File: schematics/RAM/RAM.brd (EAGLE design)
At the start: 134.9 x 102.5 mm, 31 parts

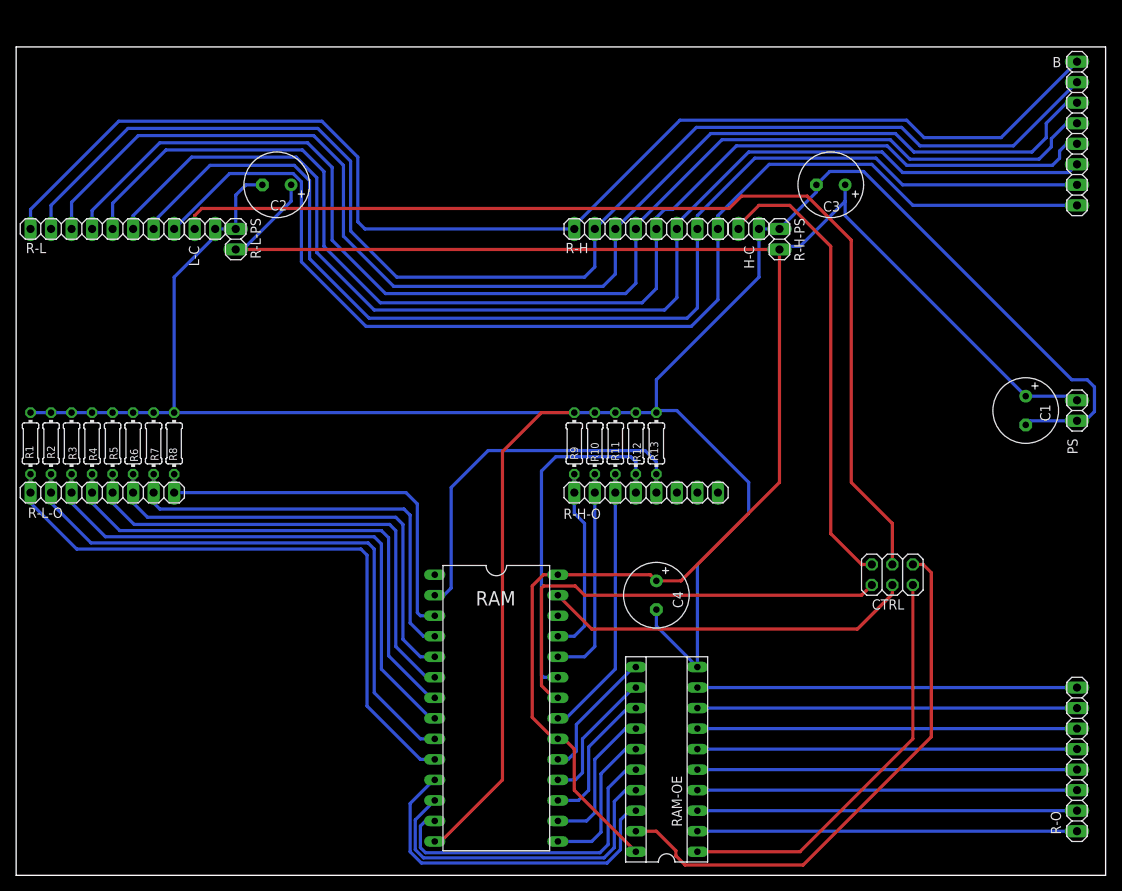
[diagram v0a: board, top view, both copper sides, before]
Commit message: RAM merged with register.
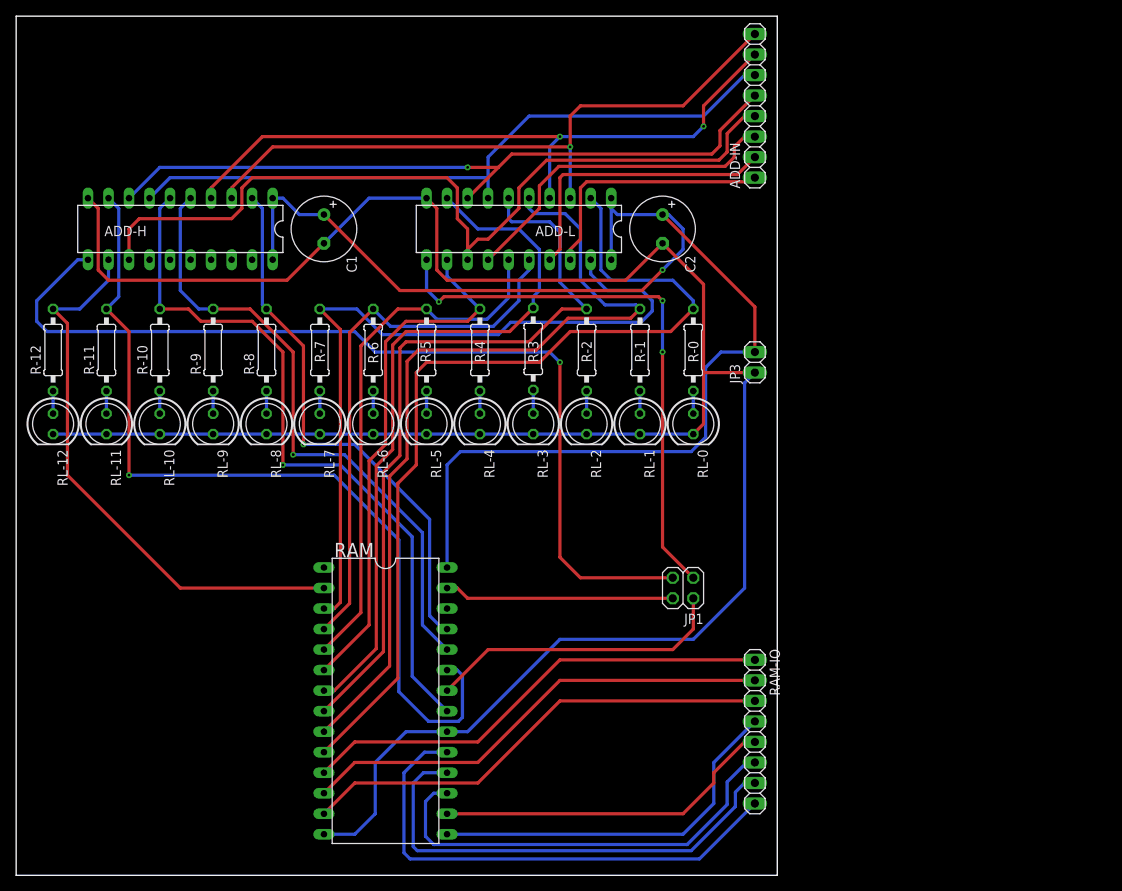
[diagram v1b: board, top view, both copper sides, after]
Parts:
- removed B, R-H, R-H-O, R-L, R-L-O, R-O: (no value), pinhead:1X08
- removed C3, C4: (no value), rcl:E3,5-8
- removed CTRL: (no value), pinhead:2X03
- removed H-C, L-C, PS, R-H-PS, R-L-PS: (no value), pinhead:1X02
- removed R1, R10, R11, R12, R13, R2, R3, R4, R5, R6, R7, R8, R9: (no value), rcl:0204/7
- removed RAM-OE: (no value), ic-package:SOCKET-20
- added ADD-H, ADD-L: 74273N, 74ttl-din:DIL20
- added ADD-IN, RAM-IO: (no value), pinhead:1X08
- added JP1: (no value), pinhead:2X02
- added JP3: (no value), pinhead:1X02
- added R-0, R-1, R-10, R-11, R-12, R-2, R-3, R-4, R-5, R-6, R-7, R-8, R-9: (no value), rcl:0207/10
- added RL-0, RL-1, RL-10, RL-11, RL-12, RL-2, RL-3, RL-4, RL-5, RL-6, RL-7, RL-8, RL-9: (no value), led:LED5MM
- RAM: device ic-package:DIL28-6 -> memory-nec:DIL28-6
- moved C1 89.7 mm to (38.1, 80.0)
- moved C2 48.1 mm to (80.0, 80.0), turned to 270 degrees
- moved RAM 13.7 mm to (45.7, 21.6)
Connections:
- removed net B0: B.8, R-H.1, R-L.1
- removed net B1: B.7, R-H.2, R-L.2
- removed net B2: B.6, R-H.3, R-L.3
- removed net B3: B.5, R-H.4, R-L.4
- removed net B4: B.4, R-H.5, R-L.5
- removed net B5: B.3, R-H.6, R-L.6
- removed net B6: B.2, R-H.7, R-L.7
- removed net B7: B.1, R-H.8, R-L.8
- removed net OE-DIR: CTRL.5, RAM-OE.1
- removed net R-H-CP: CTRL.2, H-C.2
- removed net R-L-CP: CTRL.4, L-C.2
- removed net R0: R-O.8, RAM-OE.2
- removed net R1: R-O.7, RAM-OE.3
- removed net R2: R-O.6, RAM-OE.4
- removed net R3: R-O.5, RAM-OE.5
- removed net R4: R-O.4, RAM-OE.6
- removed net R5: R-O.3, RAM-OE.7
- removed net R6: R-O.2, RAM-OE.8
- removed net R7: R-O.1, RAM-OE.9
- removed net RA0: R-L-O.1, R1.1, RAM.10
- removed net RA1: R-L-O.2, R2.1, RAM.9
- removed net RA10: R-H-O.3, R11.1, RAM.21
- removed net RA11: R-H-O.4, R12.1, RAM.23
- removed net RA12: R-H-O.5, R13.1, RAM.2
- removed net RA2: R-L-O.3, R3.1, RAM.8
- removed net RA3: R-L-O.4, R4.1, RAM.7
- removed net RA4: R-L-O.5, R5.1, RAM.6
- removed net RA5: R-L-O.6, R6.1, RAM.5
- removed net RA6: R-L-O.7, R7.1, RAM.4
- removed net RA7: R-L-O.8, R8.1, RAM.3
- removed net RA8: R-H-O.1, R9.1, RAM.25
- removed net RA9: R-H-O.2, R10.1, RAM.24
- removed net RAM-OE: CTRL.1, RAM.22
- removed net RAM0: RAM-OE.18, RAM.11
- removed net RAM1: RAM-OE.17, RAM.12
- removed net RAM2: RAM-OE.16, RAM.13
- removed net RAM3: RAM-OE.15, RAM.15
- removed net RAM4: RAM-OE.14, RAM.16
- removed net RAM5: RAM-OE.13, RAM.17
- removed net RAM6: RAM-OE.12, RAM.18
- removed net RAM7: RAM-OE.11, RAM.19
- new net ADD-H-CP: ADD-H.11, JP1.3
- new net ADD-L-CP: ADD-L.11, JP1.1
- new net BI-0: ADD-H.3, ADD-IN.8, ADD-L.3
- new net BI-1: ADD-H.4, ADD-IN.7, ADD-L.4
- new net BI-2: ADD-H.7, ADD-IN.6, ADD-L.7
- new net BI-3: ADD-H.8, ADD-IN.5, ADD-L.8
- new net BI-4: ADD-H.13, ADD-IN.4, ADD-L.13
- new net BI-5: ADD-IN.3, ADD-L.14
- new net BI-6: ADD-IN.2, ADD-L.17
- new net BI-7: ADD-IN.1, ADD-L.18
- new net BO-0: RAM-IO.1, RAM.11
- new net BO-1: RAM-IO.2, RAM.12
- new net BO-2: RAM-IO.3, RAM.13
- new net BO-3: RAM-IO.4, RAM.15
- new net BO-4: RAM-IO.5, RAM.16
- new net BO-5: RAM-IO.6, RAM.17
- new net BO-6: RAM-IO.7, RAM.18
- new net BO-7: RAM-IO.8, RAM.19
- new net N$1: R-0.1, RL-0.A
- new net N$10: R-3.1, RL-3.A
- new net N$13: R-4.1, RL-4.A
- new net N$16: R-5.1, RL-5.A
- new net N$19: R-6.1, RL-6.A
- new net N$22: R-7.1, RL-7.A
- new net N$25: R-8.1, RL-8.A
- new net N$28: R-9.1, RL-9.A
- new net N$31: R-10.1, RL-10.A
- new net N$34: R-11.1, RL-11.A
- new net N$37: R-12.1, RL-12.A
- new net N$4: R-1.1, RL-1.A
- new net N$7: R-2.1, RL-2.A
- new net RA-0: ADD-L.2, R-0.2, RAM.10
- new net RA-1: ADD-L.5, R-1.2, RAM.9
- new net RA-10: ADD-H.6, R-10.2, RAM.21
- new net RA-11: ADD-H.9, R-11.2, RAM.23
- new net RA-12: ADD-H.12, R-12.2, RAM.2
- new net RA-2: ADD-L.6, R-2.2, RAM.8
- new net RA-3: ADD-L.9, R-3.2, RAM.7
- new net RA-4: ADD-L.12, R-4.2, RAM.6
- new net RA-5: ADD-L.15, R-5.2, RAM.5
- new net RA-6: ADD-L.16, R-6.2, RAM.4
- new net RA-7: ADD-L.19, R-7.2, RAM.3
- new net RA-8: ADD-H.2, R-8.2, RAM.25
- new net RA-9: ADD-H.5, R-9.2, RAM.24
- net GND: now also ADD-H.10, ADD-L.10, JP3.1, RAM.20, RL-0.K, RL-1.K, RL-10.K, RL-11.K, RL-12.K, RL-2.K, RL-3.K, RL-4.K, RL-5.K, RL-6.K, RL-7.K, RL-8.K, RL-9.K; no longer C3.-, C4.-, H-C.1, L-C.1, PS.1, R-H-PS.1, R-L-PS.1, R1.2, R10.2, R11.2, R12.2, R13.2, R2.2, R3.2, R4.2, R5.2, R6.2, R7.2, R8.2, R9.2, RAM-OE.10
- net OE: now also JP1.2, RAM.22; no longer CTRL.6, RAM-OE.19
- net VCC: now also ADD-H.1, ADD-H.20, ADD-L.1, ADD-L.20, JP3.2; no longer C3.+, C4.+, PS.2, R-H-PS.2, R-L-PS.2, RAM-OE.20, RAM.20
- net WE: now also JP1.4; no longer CTRL.3
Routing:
- net B1: track 161.2 -> 0.00 mm
- net B2: track 159.7 -> 0.00 mm
- net B0: track 157.3 -> 0.00 mm
- net B3: track 156.2 -> 0.00 mm
- net B4: track 154.4 -> 0.00 mm
- net B5: track 149.7 -> 0.00 mm
- net B6: track 147.8 -> 0.00 mm
- net B7: track 144.8 -> 0.00 mm
- net R-L-CP: track 128.4 -> 0.00 mm
- net ADD-H-CP: track 0.00 -> 117.0 mm, vias 0 -> 1
- net RA-0: track 0.00 -> 112.7 mm
- net RA-11: track 0.00 -> 109.1 mm, vias 0 -> 1
- net RA-1: track 0.00 -> 105.5 mm
- net BI-4: track 0.00 -> 105.0 mm
- net RA-7: track 0.00 -> 95.4 mm
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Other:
- board size 134.9 x 102.5 mm -> 94.2 x 106.3 mm
